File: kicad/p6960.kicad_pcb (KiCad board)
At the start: 2 copper layers, 58 x 51 mm, 15 parts, among them J1 Conn_02x08_Counter_Clockwise, J2 Conn_02x08_Counter_Clockwise, J3 Conn_02x08_Counter_Clockwise, J4 Conn_02x08_Counter_Clockwise, J5 Conn_02x04_Counter_Clockwise

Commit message: fixed some shite
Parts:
- C1: footprint Tek:P69xx -> Tek:P6960

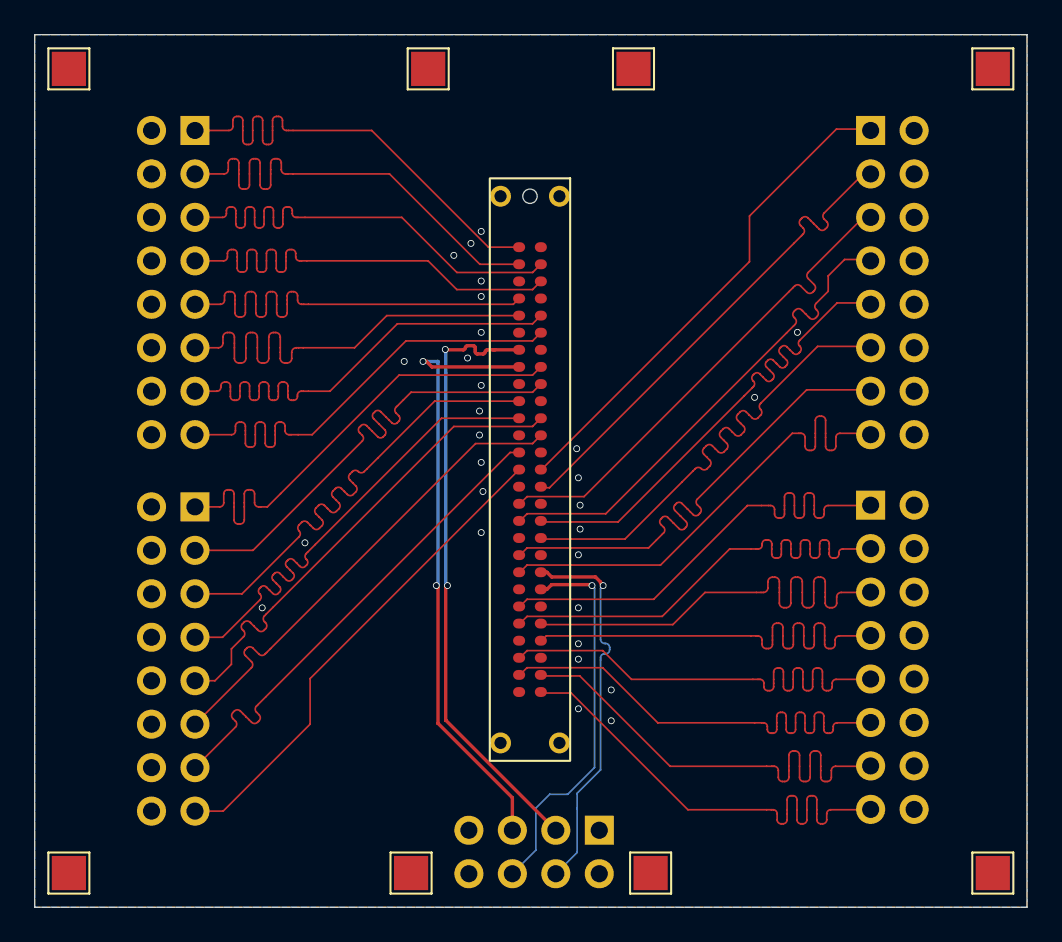
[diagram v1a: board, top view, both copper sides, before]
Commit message: Version 2.0
Changed header spacing, added real design rules (it fails), tuned all trace lengths to be 38mm, flood fill ground plane, added probe holder model, and more!
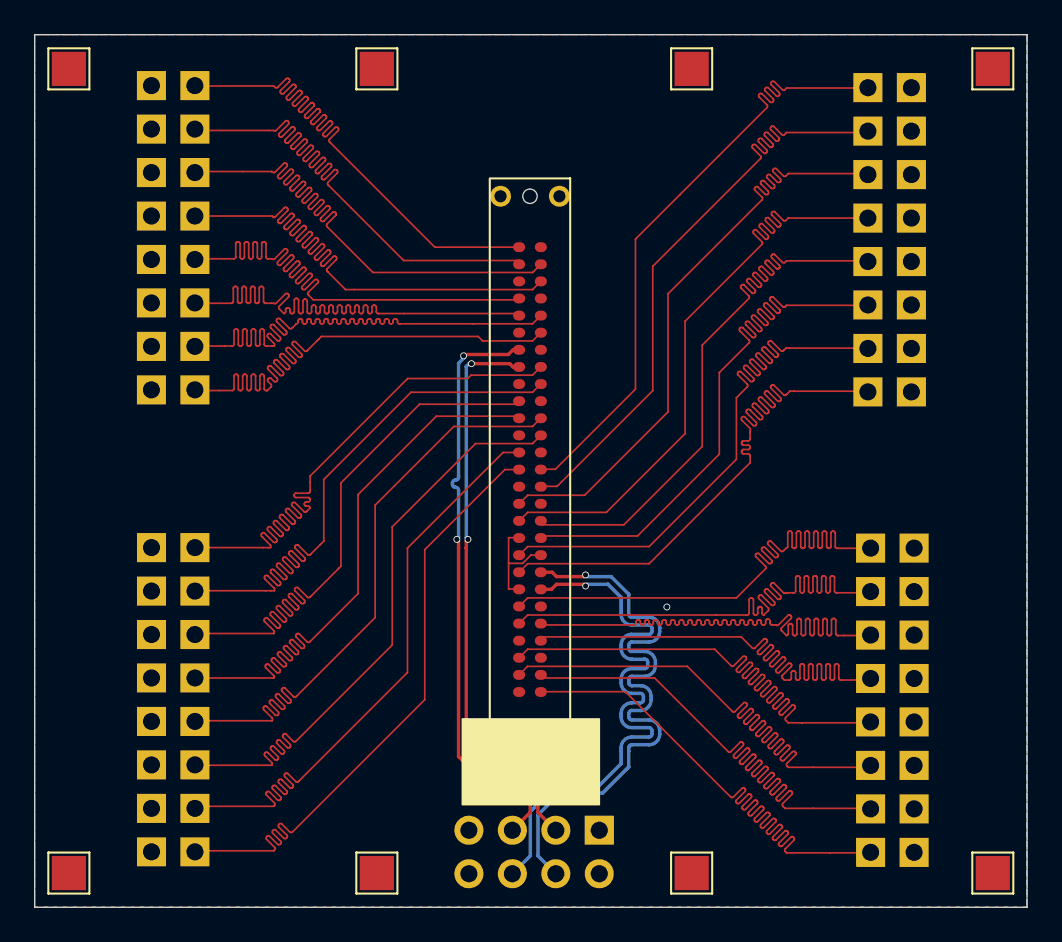
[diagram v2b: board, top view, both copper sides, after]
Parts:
- C1: footprint Tek:P6960 -> Tek:P69xx
- moved TP7 3.40 mm to (78.4, 31.0)
- moved TP5 3.00 mm to (60.0, 31.0)
- moved J1 2.62 mm to (49.4, 32.0)
- moved J4 2.51 mm to (88.9, 59.0)
- moved J3 2.51 mm to (88.7, 32.1)
- moved TP8 2.40 mm to (78.4, 78.0)
- moved J2 2.38 mm to (49.4, 59.0)
- moved TP6 2.00 mm to (60.0, 78.0)
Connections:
- J5 pad 3: CK1+ -> CK1-
- J5 pad 5: CK1- -> CK1+
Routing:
- net CK2-: track 22.6 -> 36.1 mm
- net CK2+: track 22.6 -> 35.4 mm
- net D4: track 27.6 -> 37.8 mm
- net D27: track 27.6 -> 37.8 mm
- net D21: track 28.6 -> 37.9 mm
- net D10: track 28.6 -> 37.9 mm
- net D11: track 28.7 -> 37.9 mm
- net D20: track 28.7 -> 37.9 mm
- net D9: track 28.7 -> 37.9 mm
- net D22: track 28.7 -> 37.9 mm
- net D19: track 28.7 -> 37.9 mm
- net D12: track 28.7 -> 37.9 mm
- net D3: track 28.6 -> 37.9 mm
- net D28: track 28.6 -> 37.9 mm
- net D30: track 28.6 -> 37.9 mm
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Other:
- rule pad_to_mask_clearance: 0 -> 0.0508
- board text added: "0.1524 mm / 0.1524 mm"
- board text added: "0.2540 mm"
- board text added: "1.6000 mm"
- board text added: "2"
- board text added: "58.0000 mm x 51.0000 mm"
- board text added: "BOARD CHARACTERISTICS"
- board text added: "Board Thickness:"
- board text added: "Board overall dimensions:"
- board text added: "Castellated pads:"
- board text added: "Copper Finish:"
- board text added: "Copper Layer Count:"
- board text added: "Edge card connectors:"
- board text added: "Immersion gold"
- board text added: "Impedance Control:"
- board text added: "Min hole diameter:"
- board text added: "Min track/spacing:"
- board text added: "No"
- board text added: "Plated Board Edge:"
- board text added: "Rev 2.0"
